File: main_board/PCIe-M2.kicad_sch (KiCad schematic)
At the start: 21 parts, among them J3 Bus_M.2_Socket_M, M1 M.2 Solder Nut, M2 M.2 Solder Nut, M3 M.2 Solder Nut, M4 M.2 Solder Nut, M5 M.2 Screw, U1 AP3441SHE-7B, U2 ASEK-32.768KHZ-L-R-T

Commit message: Implement part of power management.
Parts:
- C10, C11, C14, C15, C4: footprint Capacitor_SMD:C_0805_2012Metric -> Capacitor_SMD:C_0805_2012Metric_Pad1.18x1.45mm_HandSolder
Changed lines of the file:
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@@
 			)
 		)
-		(property "Footprint" "Capacitor_SMD:C_0805_2012Metric"
+		(property "Footprint" "Capacitor_SMD:C_0805_2012Metric_Pad1.18x1.45mm_HandSolder"
 			(at 153.3652 176.53 0)
 			(effects
@@
 			)
 		)
-		(property "Footprint" "Capacitor_SMD:C_0805_2012Metric"
+		(property "Footprint" "Capacitor_SMD:C_0805_2012Metric_Pad1.18x1.45mm_HandSolder"
 			(at 47.9552 175.26 0)
 			(effects
@@
 			)
 		)
-		(property "Footprint" "Capacitor_SMD:C_0805_2012Metric"
+		(property "Footprint" "Capacitor_SMD:C_0805_2012Metric_Pad1.18x1.45mm_HandSolder"
 			(at 133.0452 176.53 0)
 			(effects
@@
 			)
 		)
-		(property "Footprint" "Capacitor_SMD:C_0805_2012Metric"
+		(property "Footprint" "Capacitor_SMD:C_0805_2012Metric_Pad1.18x1.45mm_HandSolder"
 			(at 143.2052 176.53 0)
 			(effects
@@
 			)
 		)
-		(property "Footprint" "Capacitor_SMD:C_0805_2012Metric"
+		(property "Footprint" "Capacitor_SMD:C_0805_2012Metric_Pad1.18x1.45mm_HandSolder"
 			(at 163.5252 176.53 0)
 			(effects

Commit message: More power management goodness
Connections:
- net +5v renamed +5V
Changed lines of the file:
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@@
-		)
-	)
-	(label "+5v"
-		(at 34.29 167.64 0)
-		(fields_autoplaced yes)
-		(effects
-			(font
-				(size 1.27 1.27)
-			)
-			(justify left bottom)
 		)
 	)
@@
 		)
 	)
-	(hierarchical_label "+5v"
+	(hierarchical_label "+5V"
 		(shape input)
 		(at 34.29 167.64 180)

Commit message: Rev 1 draft
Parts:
- C1: footprint Capacitor_SMD:C_0805_2012Metric -> Capacitor_SMD:C_0805_2012Metric_Pad1.18x1.45mm_HandSolder
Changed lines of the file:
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@@
 			)
 		)
-		(property "Footprint" "Capacitor_SMD:C_0805_2012Metric"
+		(property "Footprint" "Capacitor_SMD:C_0805_2012Metric_Pad1.18x1.45mm_HandSolder"
 			(at 39.0652 175.26 0)
 			(effects

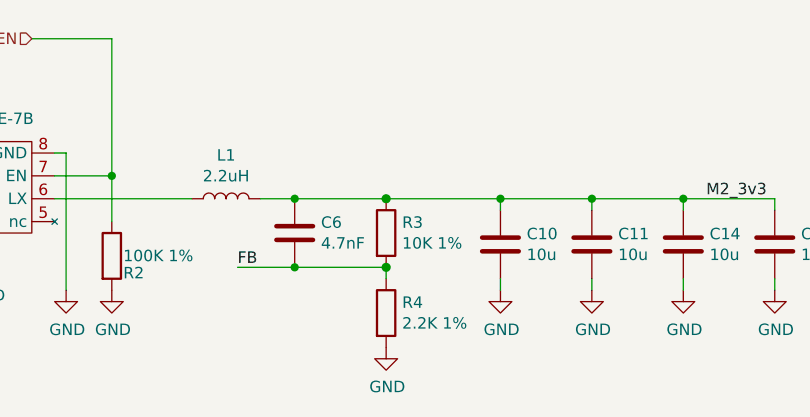
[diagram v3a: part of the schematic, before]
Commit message: Fix bad output voltage
For some reason I got 5V with previous values on prototype. Weird...
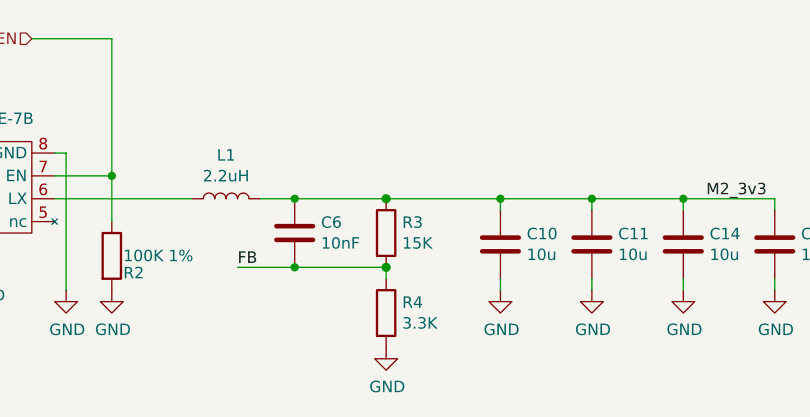
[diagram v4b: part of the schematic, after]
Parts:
- C6: value 4.7nF -> 10nF
- R3: value 10K 1% -> 15K
- R4: value 2.2K 1% -> 3.3K
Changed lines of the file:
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@@
 			)
 		)
-		(property "Value" "10K 1%"
+		(property "Value" "15K"
 			(at 121.158 172.593 0)
 			(effects
@@
 			)
 		)
-		(property "Value" "2.2K 1%"
+		(property "Value" "3.3K"
 			(at 121.158 181.483 0)
 			(effects
@@
 			)
 		)
-		(property "Value" "4.7nF"
+		(property "Value" "10nF"
 			(at 112.141 172.593 0)
 			(effects
